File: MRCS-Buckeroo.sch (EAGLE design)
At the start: 8 parts

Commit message: sent to fab
sent to fab
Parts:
- removed FRAME1: FRAME-LETTER, SparkFun-Aesthetics:FRAME-LETTER
- CON1, CON2: value (none) -> DC PWR
- CON3: value (none) -> output bypass
- CON4: value (none) -> GND BYPASS
- OUTPUT+: value CONNECTOR-M12LOCK -> OUTPUT+
- OUTPUT-: value CONNECTOR-M12LOCK -> OUTPUT-
- renumbered GND to OUTPUT-, OUTPUT to OUTPUT+
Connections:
- net N$1 renamed INPUT+
- net N$2 renamed GND
- net N$3 renamed OUTPUT-
- net N$4 renamed OUTPUT+
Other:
- note added: "Input+ GND"
- note added: "Output+"
- note removed: "+Input GND"
- note removed: "Output"
- moved on the sheet: CON4
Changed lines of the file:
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@@
 </classes>
 <parts>
-<part name="OUTPUT" library="SPCoast" deviceset="CONNECTOR-M12" device="LOCK"/>
-<part name="GND" library="SPCoast" deviceset="CONNECTOR-M12" device="LOCK"/>
-<part name="CON1" library="SPCoast" deviceset="CONNECTOR-DC-POWER" device="-RA"/>
-<part name="CON2" library="SPCoast" deviceset="CONNECTOR-M02" device="3.5MM-LOCK"/>
+<part name="OUTPUT+" library="SPCoast" deviceset="CONNECTOR-M12" device="LOCK" value="OUTPUT+"/>
+<part name="OUTPUT-" library="SPCoast" deviceset="CONNECTOR-M12" device="LOCK" value="OUTPUT-"/>
+<part name="CON1" library="SPCoast" deviceset="CONNECTOR-DC-POWER" device="-RA" value="DC PWR"/>
+<part name="CON2" library="SPCoast" deviceset="CONNECTOR-M02" device="3.5MM-LOCK" value="DC PWR"/>
 <part name="U$4" library="diy-modules" deviceset="DC-DC-STEP-DOWN-LM2596" device=""/>
-<part name="FRAME1" library="SparkFun-Aesthetics" deviceset="FRAME-LETTER" device=""/>
-<part name="CON3" library="SPCoast" deviceset="CONNECTOR-M02" device="MOLEX-1X02-LOCK"/>
-<part name="CON4" library="SPCoast" deviceset="CONNECTOR-M02" device="MOLEX-1X02-LOCK"/>
+<part name="CON3" library="SPCoast" deviceset="CONNECTOR-M02" device="MOLEX-1X02-LOCK" value="output bypass"/>
+<part name="CON4" library="SPCoast" deviceset="CONNECTOR-M02" device="MOLEX-1X02-LOCK" value="GND BYPASS"/>
 </parts>
 <sheets>
 <sheet>
 <plain>
-<text x="119.38" y="81.28" size="2.54" layer="97" rot="R90">Output</text>
-<text x="109.22" y="43.18" size="1.778" layer="97">+Input
+<text x="119.38" y="81.28" size="2.54" layer="97" rot="R90">Output+</text>
+<text x="109.22" y="43.18" size="1.778" layer="97">Input+
 GND
 </text>
@@
 </plain>
 <instances>
-<instance part="OUTPUT" gate="G$1" x="119.38" y="96.52" smashed="yes" rot="MR180">
+<instance part="OUTPUT+" gate="G$1" x="119.38" y="96.52" smashed="yes" rot="MR180">
 <attribute name="VALUE" x="99.06" y="124.46" size="1.778" layer="96" rot="MR180"/>
 <attribute name="NAME" x="119.38" y="80.518" size="1.778" layer="95" rot="MR180"/>
 </instance>
-<instance part="GND" gate="G$1" x="190.5" y="96.52" smashed="yes" rot="R180">
-<attribute name="VALUE" x="175.26" y="111.76" size="1.778" layer="96" rot="R270"/>
-<attribute name="NAME" x="190.5" y="80.518" size="1.778" layer="95" rot="R180"/>
+<instance part="OUTPUT-" gate="G$1" x="190.5" y="96.52" smashed="yes" rot="R180">
+<attribute name="VALUE" x="193.04" y="111.76" size="1.778" layer="96" rot="R270"/>
+<attribute name="NAME" x="190.5" y="77.978" size="1.778" layer="95" rot="R180"/>
 </instance>
 <instance part="CON1" gate="J" x="121.92" y="22.86"/>
 <instance part="CON2" gate="J" x="124.46" y="45.72"/>
 <instance part="U$4" gate="G$1" x="157.48" y="43.18"/>
-<instance part="FRAME1" gate="G$1" x="58.42" y="-48.26"/>
-<instance part="FRAME1" gate="G$2" x="205.74" y="-48.26"/>
 <instance part="CON3" gate="J" x="154.94" y="68.58" rot="R270"/>
-<instance part="CON4" gate="J" x="160.02" y="22.86" rot="R90"/>
+<instance part="CON4" gate="J" x="157.48" y="22.86" rot="R90"/>
 </instances>
 <busses>
 </busses>
 <nets>
-<net name="N$3" class="1">
+<net name="OUTPUT-" class="1">
 <segment>
-<pinref part="GND" gate="G$1" pin="12"/>
+<pinref part="OUTPUT-" gate="G$1" pin="12"/>
+<wire x1="180.34" y1="27.94" x2="180.34" y2="38.1" width="0.6096" layer="91"/>
+<pinref part="OUTPUT-" gate="G$1" pin="11"/>
 <wire x1="180.34" y1="38.1" x2="180.34" y2="83.82" width="0.6096" layer="91"/>
-<pinref part="GND" gate="G$1" pin="11"/>
 <wire x1="180.34" y1="83.82" x2="180.34" y2="86.36" width="0.6096" layer="91"/>
-<pinref part="GND" gate="G$1" pin="10"/>
+<pinref part="OUTPUT-" gate="G$1" pin="10"/>
 <wire x1="180.34" y1="86.36" x2="180.34" y2="88.9" width="0.6096" layer="91"/>
-<pinref part="GND" gate="G$1" pin="9"/>
+<pinref part="OUTPUT-" gate="G$1" pin="9"/>
 <wire x1="180.34" y1="88.9" x2="180.34" y2="91.44" width="0.6096" layer="91"/>
-<pinref part="GND" gate="G$1" pin="8"/>
+<pinref part="OUTPUT-" gate="G$1" pin="8"/>
 <wire x1="180.34" y1="91.44" x2="180.34" y2="93.98" width="0.6096" layer="91"/>
-<pinref part="GND" gate="G$1" pin="7"/>
+<pinref part="OUTPUT-" gate="G$1" pin="7"/>
 <wire x1="180.34" y1="93.98" x2="180.34" y2="96.52" width="0.6096" layer="91"/>
-<pinref part="GND" gate="G$1" pin="6"/>
+<pinref part="OUTPUT-" gate="G$1" pin="6"/>
 <wire x1="180.34" y1="96.52" x2="180.34" y2="99.06" width="0.6096" layer="91"/>
-<pinref part="GND" gate="G$1" pin="5"/>
+<pinref part="OUTPUT-" gate="G$1" pin="5"/>
 <wire x1="180.34" y1="99.06" x2="180.34" y2="101.6" width="0.6096" layer="91"/>
-<pinref part="GND" gate="G$1" pin="4"/>
+<pinref part="OUTPUT-" gate="G$1" pin="4"/>
 <wire x1="180.34" y1="101.6" x2="180.34" y2="104.14" width="0.6096" layer="91"/>
-<pinref part="GND" gate="G$1" pin="3"/>
+<pinref part="OUTPUT-" gate="G$1" pin="3"/>
 <wire x1="180.34" y1="104.14" x2="180.34" y2="106.68" width="0.6096" layer="91"/>
-<pinref part="GND" gate="G$1" pin="2"/>
+<pinref part="OUTPUT-" gate="G$1" pin="2"/>
 <wire x1="180.34" y1="106.68" x2="180.34" y2="109.22" width="0.6096" layer="91"/>
-<pinref part="GND" gate="G$1" pin="1"/>
+<pinref part="OUTPUT-" gate="G$1" pin="1"/>
 <wire x1="180.34" y1="109.22" x2="180.34" y2="111.76" width="0.6096" layer="91"/>
 <junction x="180.34" y="83.82"/>
@@
 <junction x="180.34" y="111.76"/>
 <pinref part="U$4" gate="G$1" pin="OUT-"/>
-<wire x1="180.34" y1="38.1" x2="175.26" y2="38.1" width="0.6096" layer="91"/>
+<wire x1="175.26" y1="38.1" x2="180.34" y2="38.1" width="0.6096" layer="91"/>
 <pinref part="CON4" gate="J" pin="A"/>
-<wire x1="160.02" y1="27.94" x2="180.34" y2="27.94" width="0.6096" layer="91"/>
-<wire x1="180.34" y1="27.94" x2="180.34" y2="38.1" width="0.6096" layer="91"/>
+<wire x1="157.48" y1="27.94" x2="180.34" y2="27.94" width="0.6096" layer="91"/>
 <junction x="180.34" y="27.94"/>
 <junction x="180.34" y="38.1"/>
 </segment>
 </net>
-<net name="N$4" class="1">
+<net name="OUTPUT+" class="1">
 <segment>
-<pinref part="OUTPUT" gate="G$1" pin="1"/>
+<pinref part="OUTPUT+" gate="G$1" pin="1"/>
 <junction x="129.54" y="111.76"/>
-<pinref part="OUTPUT" gate="G$1" pin="2"/>
+<pinref part="OUTPUT+" gate="G$1" pin="2"/>
 <wire x1="129.54" y1="109.22" x2="129.54" y2="111.76" width="0.6096" layer="91"/>
 <junction x="129.54" y="109.22"/>
-<pinref part="OUTPUT" gate="G$1" pin="3"/>
+<pinref part="OUTPUT+" gate="G$1" pin="3"/>
 <wire x1="129.54" y1="106.68" x2="129.54" y2="109.22" width="0.6096" layer="91"/>
 <junction x="129.54" y="106.68"/>
-<pinref part="OUTPUT" gate="G$1" pin="4"/>
+<pinref part="OUTPUT+" gate="G$1" pin="4"/>
 <wire x1="129.54" y1="104.14" x2="129.54" y2="106.68" width="0.6096" layer="91"/>
-<pinref part="OUTPUT" gate="G$1" pin="5"/>
+<pinref part="OUTPUT+" gate="G$1" pin="5"/>
 <wire x1="129.54" y1="104.14" x2="129.54" y2="101.6" width="0.6096" layer="91"/>
-<pinref part="OUTPUT" gate="G$1" pin="6"/>
+<pinref part="OUTPUT+" gate="G$1" pin="6"/>
 <wire x1="129.54" y1="101.6" x2="129.54" y2="99.06" width="0.6096" layer="91"/>
-<pinref part="OUTPUT" gate="G$1" pin="7"/>
+<pinref part="OUTPUT+" gate="G$1" pin="7"/>
 <wire x1="129.54" y1="99.06" x2="129.54" y2="96.52" width="0.6096" layer="91"/>
-<pinref part="OUTPUT" gate="G$1" pin="8"/>
+<pinref part="OUTPUT+" gate="G$1" pin="8"/>
 <wire x1="129.54" y1="96.52" x2="129.54" y2="93.98" width="0.6096" layer="91"/>
-<pinref part="OUTPUT" gate="G$1" pin="12"/>
-<pinref part="OUTPUT" gate="G$1" pin="11"/>
+<pinref part="OUTPUT+" gate="G$1" pin="12"/>
+<pinref part="OUTPUT+" gate="G$1" pin="11"/>
 <wire x1="129.54" y1="83.82" x2="129.54" y2="86.36" width="0.6096" layer="91"/>
-<pinref part="OUTPUT" gate="G$1" pin="10"/>
+<pinref part="OUTPUT+" gate="G$1" pin="10"/>
 <wire x1="129.54" y1="86.36" x2="129.54" y2="88.9" width="0.6096" layer="91"/>
-<pinref part="OUTPUT" gate="G$1" pin="9"/>
+<pinref part="OUTPUT+" gate="G$1" pin="9"/>
 <wire x1="129.54" y1="88.9" x2="129.54" y2="91.44" width="0.6096" layer="91"/>
 <junction x="129.54" y="83.82"/>
@@
 </segment>
 </net>
-<net name="N$1" class="0">
+<net name="INPUT+" class="0">
 <segment>
 <pinref part="CON2" gate="J" pin="B"/>
@@
 </segment>
 </net>
-<net name="N$2" class="0">
+<net name="GND" class="0">
 <segment>
 <pinref part="CON2" gate="J" pin="A"/>
@@
 <pinref part="CON4" gate="J" pin="B"/>
 <wire x1="137.16" y1="27.94" x2="137.16" y2="38.1" width="0.6096" layer="91"/>
-<wire x1="157.48" y1="27.94" x2="137.16" y2="27.94" width="0.6096" layer="91"/>
+<wire x1="154.94" y1="27.94" x2="137.16" y2="27.94" width="0.6096" layer="91"/>
 <junction x="137.16" y="27.94"/>
 </segment>

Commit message: Update MRCS-Buckeroo.sch
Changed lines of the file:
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@@
 <part name="CON3" library="SPCoast" deviceset="CONNECTOR-M02" device="MOLEX-1X02-LOCK" value="output bypass"/>
 <part name="CON4" library="SPCoast" deviceset="CONNECTOR-M02" device="MOLEX-1X02-LOCK" value="GND BYPASS"/>
+<part name="FRAME1" library="frames" deviceset="FRAME_A_L" device=""/>
 </parts>
 <sheets>
@@
 </text>
 <text x="210.82" y="-40.64" size="3.81" layer="97">Seth Neumann</text>
+<text x="152.4" y="-12.7" size="3.81" layer="97" font="vector">Seth Neumann</text>
 </plain>
 <instances>
 <instance part="OUTPUT+" gate="G$1" x="119.38" y="96.52" smashed="yes" rot="MR180">
-<attribute name="VALUE" x="99.06" y="124.46" size="1.778" layer="96" rot="MR180"/>
+<attribute name="VALUE" x="116.84" y="119.38" size="1.778" layer="96" rot="MR180"/>
 <attribute name="NAME" x="119.38" y="80.518" size="1.778" layer="95" rot="MR180"/>
 </instance>
@@
 <instance part="CON3" gate="J" x="154.94" y="68.58" rot="R270"/>
 <instance part="CON4" gate="J" x="157.48" y="22.86" rot="R90"/>
+<instance part="FRAME1" gate="G$1" x="-66.04" y="-30.48"/>
+<instance part="FRAME1" gate="G$2" x="106.68" y="-30.48"/>
 </instances>
 <busses>

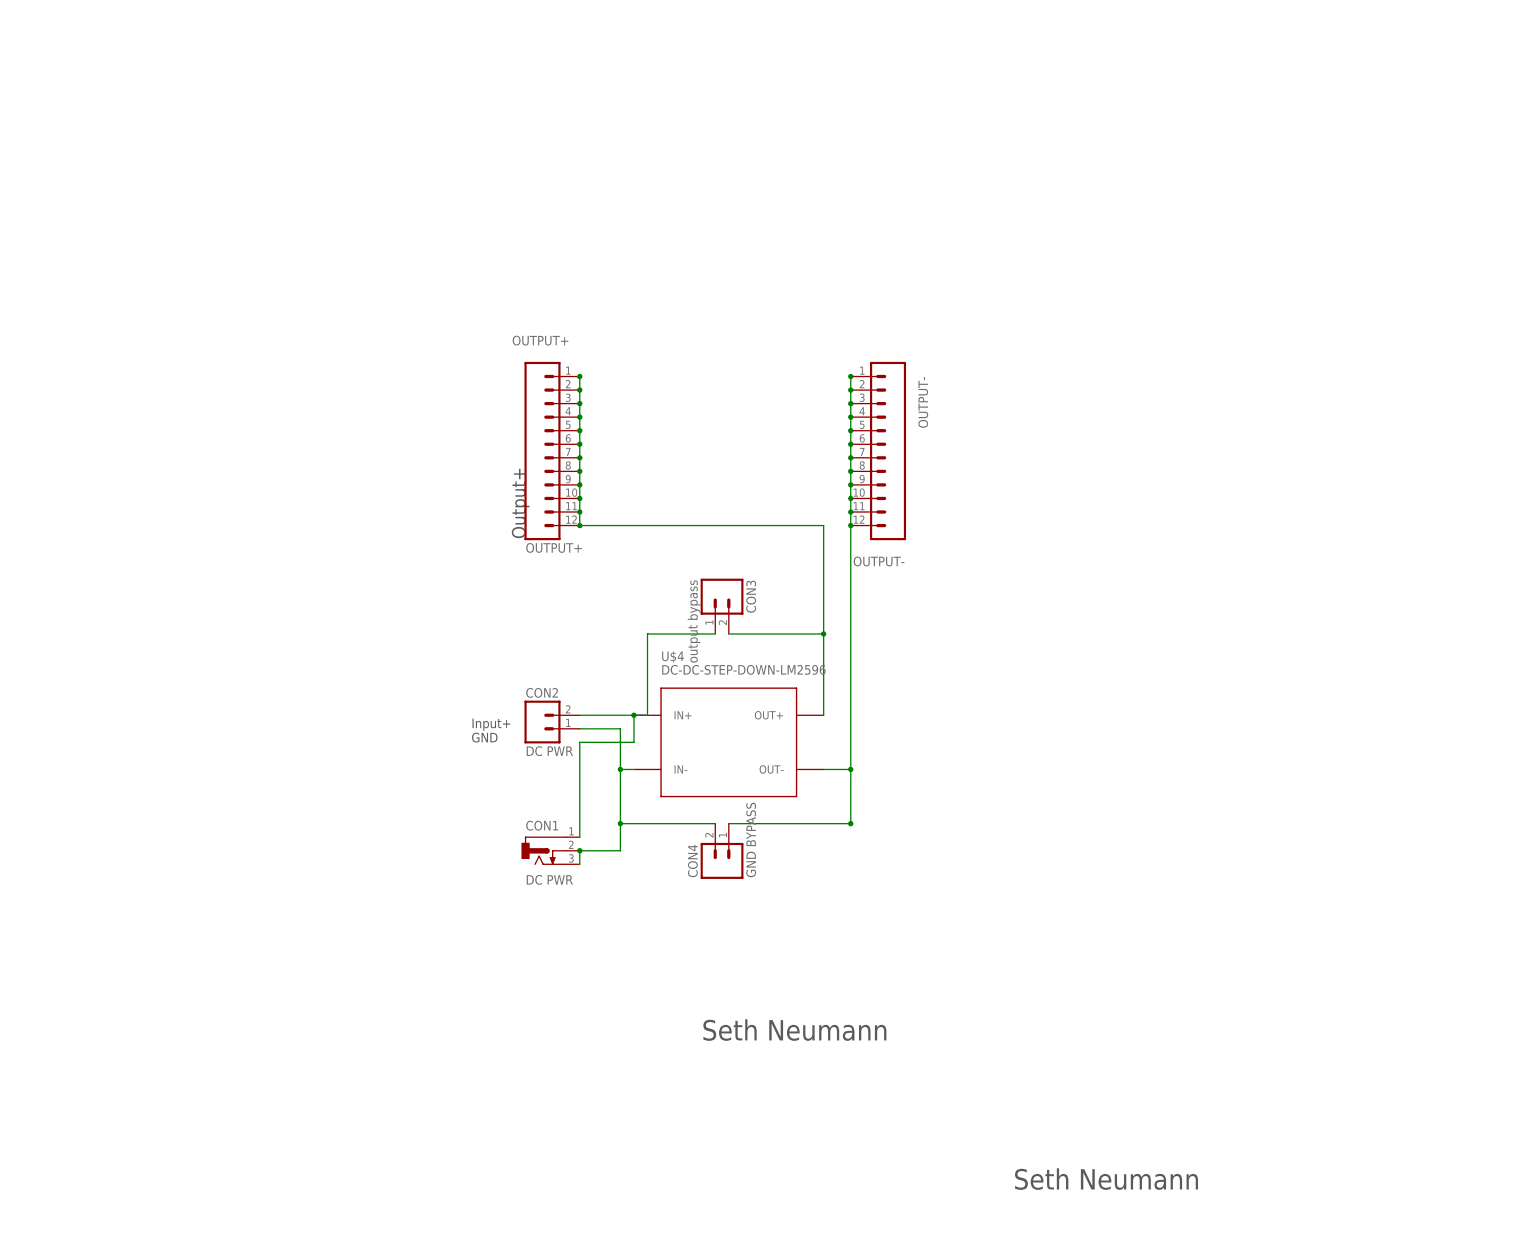
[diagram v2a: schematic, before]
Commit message: Added regulator options
Supports MH-Mini-360 bucking converter and 780X TO-220 linear regulators
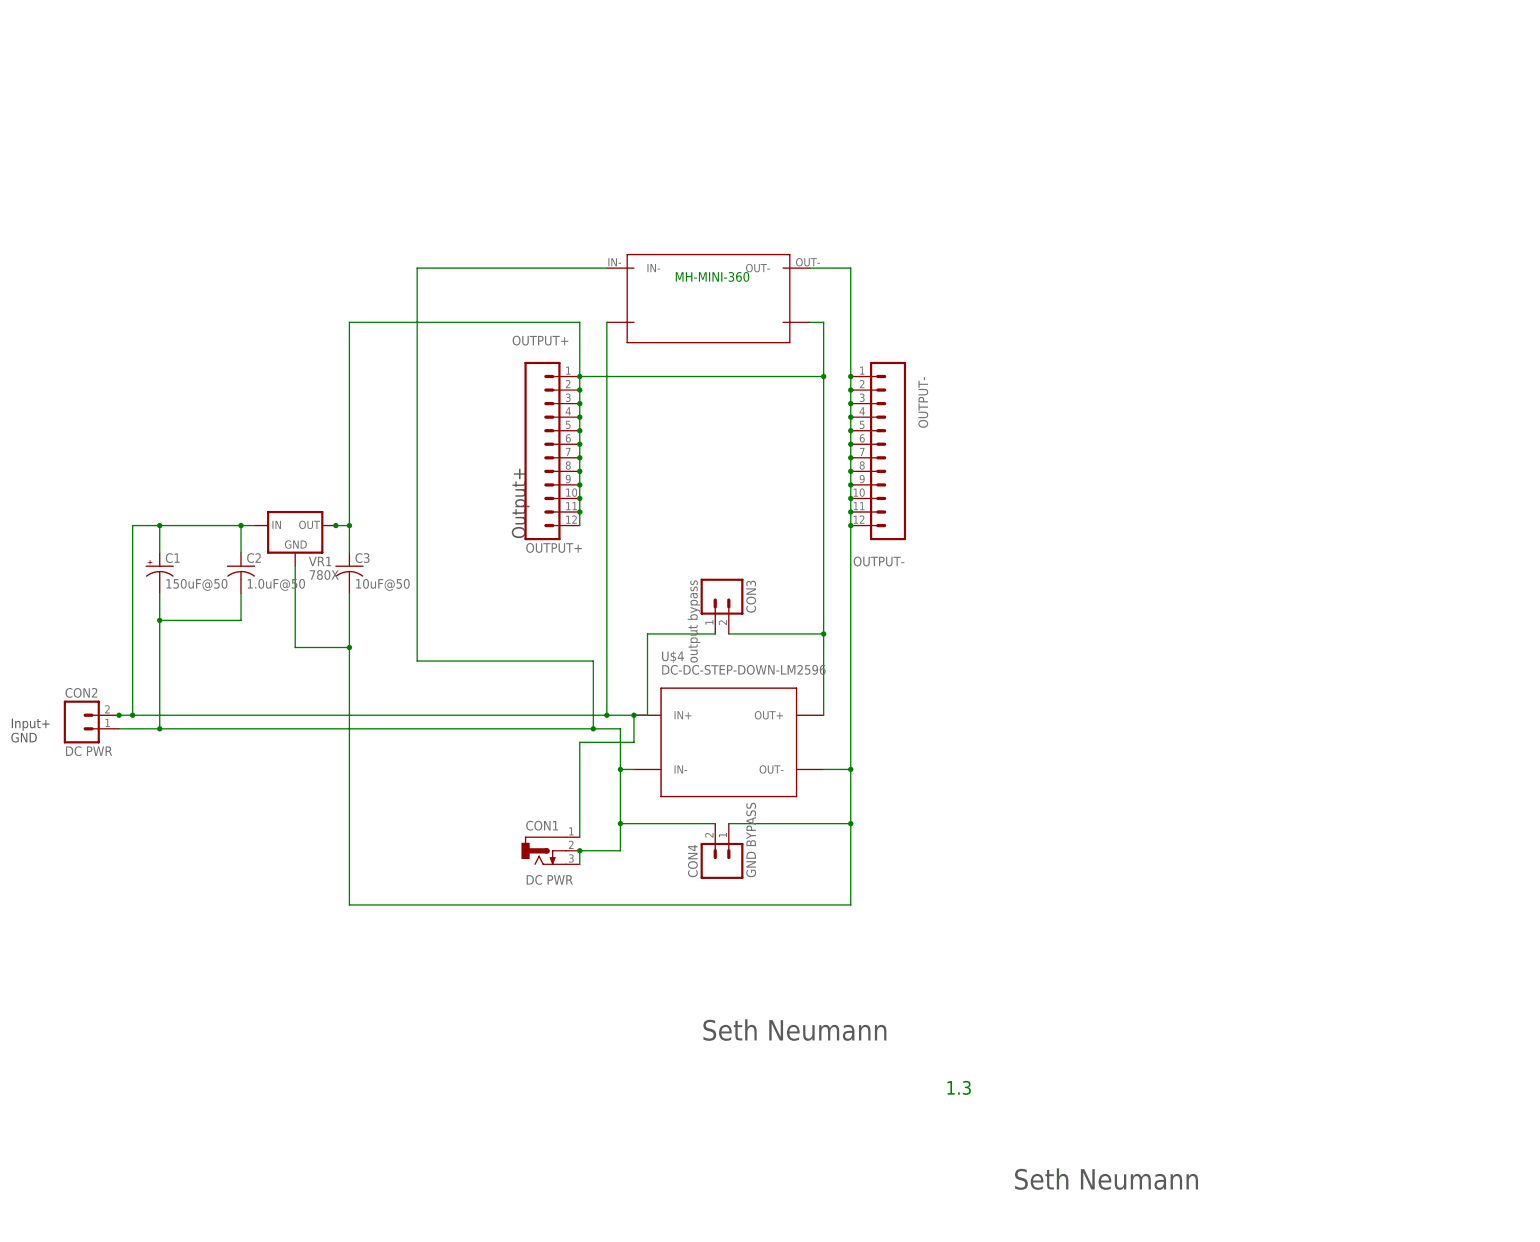
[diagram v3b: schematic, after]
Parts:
- added C1: 150uF@50, SPCoast:CAP-POLPTH-5MM
- added C2: 1.0uF@50, SPCoast:CAPPTH2
- added C3: 10uF@50, SPCoast:CAPPTH2
- added MH-MINI-360: MH-MINI-360, MH-MINI-360:MH-MINI-360
- added VR1: 780X, SPCoast:VREG-PTH-RA-
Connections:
- net GND: now also C1.-, C2.2, MH-MINI-360.IN-
- net INPUT+: now also C1.+, C2.1, MH-MINI-360.INN+, VR1.IN
- net OUTPUT+: now also C3.1, MH-MINI-360.OUTT+, VR1.OUT
- net OUTPUT-: now also C3.2, MH-MINI-360.OUT-, VR1.GND
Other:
- note added: "1.3"
- note added: "MH-MINI-360"
- moved on the sheet: CON2

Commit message: Release 3 sent out for fab
These include the mini bucker and an updown bucker as well as the pads for 780X TO220 packages. These need to be tested before panelization.
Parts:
- added U$5: XL6009BOARD, MRCS:XL6009BOARD
- MH-MINI-360: device MH-MINI-360:MH-MINI-360 -> MRCS:MH-MINI-360
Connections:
- net GND: now also U$5.IN-
- net INPUT+: now also U$5.IN+
- net OUTPUT+: now also U$5.OUT+
- net OUTPUT-: now also U$5.OUT-
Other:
- note added: "1.4"
- note removed: "1.3"
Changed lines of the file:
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@@
 <part name="CON4" library="SPCoast" deviceset="CONNECTOR-M02" device="MOLEX-1X02-LOCK" value="GND BYPASS"/>
 <part name="FRAME1" library="frames" deviceset="FRAME_A_L" device=""/>
-<part name="MH-MINI-360" library="MH-MINI-360" deviceset="MH-MINI-360" device=""/>
+<part name="MH-MINI-360" library="MRCS" deviceset="MH-MINI-360" device=""/>
 <part name="C1" library="SPCoast" deviceset="CAP-POL*" device="PTH-5MM" value="150uF@50"/>
 <part name="C2" library="SPCoast" deviceset="CAP*" device="PTH2" value="1.0uF@50"/>
 <part name="C3" library="SPCoast" deviceset="CAP*" device="PTH2" value="10uF@50"/>
 <part name="VR1" library="SPCoast" deviceset="VREG-?-*" device="PTH-RA" value="780X"/>
+<part name="U$5" library="MRCS" deviceset="XL6009BOARD" device=""/>
 </parts>
 <sheets>
@@
 <text x="152.4" y="-12.7" size="3.81" layer="97" font="vector">Seth Neumann</text>
 <text x="147.32" y="129.54" size="1.778" layer="91">MH-MINI-360</text>
-<text x="198.12" y="-22.86" size="2.54" layer="91">1.3</text>
+<text x="198.12" y="-22.86" size="2.54" layer="91">1.4</text>
 </plain>
 <instances>
@@
 <instance part="C3" gate="C1" x="86.36" y="76.2"/>
 <instance part="VR1" gate="VR" x="76.2" y="83.82"/>
+<instance part="U$5" gate="G$1" x="142.24" y="151.13"/>
 </instances>
 <busses>
@@
 <wire x1="76.2" y1="60.96" x2="86.36" y2="60.96" width="0.6096" layer="91"/>
 <junction x="86.36" y="60.96"/>
+<wire x1="180.34" y1="132.08" x2="190.5" y2="132.08" width="0.6096" layer="91"/>
+<wire x1="190.5" y1="132.08" x2="190.5" y2="143.51" width="0.6096" layer="91"/>
+<wire x1="190.5" y1="143.51" x2="186.69" y2="143.51" width="0.6096" layer="91"/>
+<junction x="180.34" y="132.08"/>
+<pinref part="U$5" gate="G$1" pin="OUT-"/>
 </segment>
 </net>
@@
 <junction x="83.82" y="83.82"/>
 <junction x="86.36" y="83.82"/>
+<wire x1="86.36" y1="121.92" x2="86.36" y2="180.34" width="0.6096" layer="91"/>
+<wire x1="86.36" y1="180.34" x2="187.96" y2="180.34" width="0.6096" layer="91"/>
+<wire x1="187.96" y1="180.34" x2="187.96" y2="172.72" width="0.6096" layer="91"/>
+<wire x1="187.96" y1="172.72" x2="186.69" y2="172.72" width="0.6096" layer="91"/>
+<pinref part="U$5" gate="G$1" pin="OUT+"/>
+<junction x="86.36" y="121.92"/>
 </segment>
 </net>
@@
 <wire x1="66.04" y1="83.82" x2="68.58" y2="83.82" width="0.6096" layer="91"/>
 <junction x="66.04" y="83.82"/>
+<wire x1="45.72" y1="83.82" x2="45.72" y2="171.45" width="0.6096" layer="91"/>
+<wire x1="45.72" y1="171.45" x2="106.68" y2="171.45" width="0.6096" layer="91"/>
+<pinref part="U$5" gate="G$1" pin="IN+"/>
+<junction x="45.72" y="83.82"/>
 </segment>
 </net>
@@
 <wire x1="66.04" y1="66.04" x2="50.8" y2="66.04" width="0.6096" layer="91"/>
 <junction x="50.8" y="66.04"/>
-</segment>
-</net>
+<wire x1="99.06" y1="132.08" x2="99.06" y2="143.51" width="0.6096" layer="91"/>
+<pinref part="U$5" gate="G$1" pin="IN-"/>
+<wire x1="99.06" y1="143.51" x2="106.68" y2="143.51" width="0.6096" layer="91"/>
+<junction x="99.06" y="132.08"/>
+</segment>
+</net>
